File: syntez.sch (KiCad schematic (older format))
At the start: 14 parts, among them J12 USB_B_Mini, J15 IO, U1 SI5351A, Y2 Crystal

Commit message: add I2S_CLKIN_MCU
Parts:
- removed J12: USB_B_Mini, Connect:USB_Mini-B, symbol USB_B_Mini
- removed RN4: 47, Resistors_SMD:R_Array_Convex_4x0603, symbol R_Pack04
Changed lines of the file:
@@
 $Descr A4 11693 8268
 encoding utf-8
-Sheet 2 6
+Sheet 2 5
 Title ""
 Date ""
@@
 	3150 1500 3150 2250
 $Comp
-L +3V3 #PWR13
+L +3V3 #PWR011
 U 1 1 5DDEDF62
 P 3150 1500
-F 0 "#PWR13" H 3150 1350 50  0001 C CNN
+F 0 "#PWR011" H 3150 1350 50  0001 C CNN
 F 1 "+3V3" H 3150 1640 50  0000 C CNN
 F 2 "" H 3150 1500 50  0001 C CNN
@@
 	3000 2900 2550 2900
 $Comp
-L GND #PWR12
+L GND #PWR012
 U 1 1 5DDEE4A0
 P 2750 1800
-F 0 "#PWR12" H 2750 1550 50  0001 C CNN
+F 0 "#PWR012" H 2750 1550 50  0001 C CNN
 F 1 "GND" H 2750 1650 50  0001 C CNN
 F 2 "" H 2750 1800 50  0001 C CNN
@@
 $EndComp
 $Comp
-L GND #PWR14
+L GND #PWR013
 U 1 1 5DDEE4E1
 P 4750 2450
-F 0 "#PWR14" H 4750 2200 50  0001 C CNN
+F 0 "#PWR013" H 4750 2200 50  0001 C CNN
 F 1 "GND" H 4750 2300 50  0001 C CNN
 F 2 "" H 4750 2450 50  0001 C CNN
@@
 $EndComp
 $Comp
-L +3V3 #PWR15
+L +3V3 #PWR014
 U 1 1 5DDEE519
 P 4750 2550
-F 0 "#PWR15" H 4750 2400 50  0001 C CNN
+F 0 "#PWR014" H 4750 2400 50  0001 C CNN
 F 1 "+3V3" V 4750 2800 50  0000 C CNN
 F 2 "" H 4750 2550 50  0001 C CNN
@@
 Connection ~ 6100 1100
 $Comp
-L GND #PWR16
+L GND #PWR015
 U 1 1 5DDEEBF2
 P 6100 1400
-F 0 "#PWR16" H 6100 1150 50  0001 C CNN
+F 0 "#PWR015" H 6100 1150 50  0001 C CNN
 F 1 "GND" H 6100 1250 50  0001 C CNN
 F 2 "" H 6100 1400 50  0001 C CNN
@@
 $EndComp
 $Comp
-L GND #PWR17
+L GND #PWR016
 U 1 1 5DDEEC35
 P 6100 2150
-F 0 "#PWR17" H 6100 1900 50  0001 C CNN
+F 0 "#PWR016" H 6100 1900 50  0001 C CNN
 F 1 "GND" H 6100 2000 50  0001 C CNN
 F 2 "" H 6100 2150 50  0001 C CNN
@@
 	6100 2650 6100 2750
 $Comp
-L GND #PWR18
+L GND #PWR017
 U 1 1 5DDEECF7
 P 6100 2950
-F 0 "#PWR18" H 6100 2700 50  0001 C CNN
+F 0 "#PWR017" H 6100 2700 50  0001 C CNN
 F 1 "GND" H 6100 2800 50  0001 C CNN
 F 2 "" H 6100 2950 50  0001 C CNN
@@
 Text GLabel 8000 3600 0    60   Input ~ 0
 IO0
-Text GLabel 4400 6100 2    60   Input ~ 0
-I2C_SCL_MCU
-Text GLabel 4400 6300 2    60   BiDi ~ 0
-I2C_SDA_MCU
-Text GLabel 3200 5600 0    60   Output ~ 0
-I2C_SCL
-Text GLabel 3200 5800 0    60   BiDi ~ 0
-I2C_SDA
-$Comp
-L USB_B_Mini J12
-U 1 1 5DE4C0D6
-P 2200 6400
-F 0 "J12" H 2000 6850 50  0000 L CNN
-F 1 "USB_B_Mini" H 2000 6750 50  0000 L CNN
-F 2 "Connect:USB_Mini-B" H 2350 6350 50  0001 C CNN
-F 3 "" H 2350 6350 50  0001 C CNN
-	1    2200 6400
-	1    0    0    -1
-$EndComp
-Wire Wire Line
-	4200 6400 4200 6700
-Wire Wire Line
-	4200 6700 4400 6700
-Text GLabel 4400 6700 2    60   BiDi ~ 0
-USB_DM
-Text GLabel 4400 6500 2    60   BiDi ~ 0
-USB_DP
-$Comp
-L GND #PWR11
-U 1 1 5DE4C0F5
-P 2200 6900
-F 0 "#PWR11" H 2200 6650 50  0001 C CNN
-F 1 "GND" H 2200 6750 50  0000 C CNN
-F 2 "" H 2200 6900 50  0001 C CNN
-F 3 "" H 2200 6900 50  0001 C CNN
-	1    2200 6900
-	1    0    0    -1
-$EndComp
-$Comp
-L R_Pack04 RN4
-U 1 1 5DE4C1DE
-P 3850 6400
-F 0 "RN4" V 3550 6400 50  0000 C CNN
-F 1 "47" V 4050 6400 50  0000 C CNN
-F 2 "Resistors_SMD:R_Array_Convex_4x0603" V 4125 6400 50  0001 C CNN
-F 3 "" H 3850 6400 50  0001 C CNN
-	1    3850 6400
-	0    1    1    0
-$EndComp
-Wire Wire Line
-	4050 6500 4400 6500
-Wire Wire Line
-	4050 6300 4400 6300
-Wire Wire Line
-	3200 5800 3300 5800
-Wire Wire Line
-	3300 5800 3300 6300
-Wire Wire Line
-	3300 6300 3650 6300
-Wire Wire Line
-	2200 6800 2200 6900
-Wire Wire Line
-	2100 6800 2100 6850
-Wire Wire Line
-	2100 6850 2200 6850
-Connection ~ 2200 6850
-Wire Wire Line
-	3200 5600 3400 5600
-Wire Wire Line
-	3400 5600 3400 6200
-Wire Wire Line
-	3400 6200 3650 6200
-Wire Wire Line
-	4400 6100 4300 6100
-Wire Wire Line
-	4300 6100 4300 6200
-Wire Wire Line
-	4300 6200 4050 6200
-Wire Wire Line
-	4050 6400 4200 6400
-Wire Wire Line
-	3650 6400 3050 6400
-Wire Wire Line
-	3050 6400 3050 6500
-Wire Wire Line
-	3050 6500 2500 6500
-Wire Wire Line
-	2500 6400 2850 6400
-Wire Wire Line
-	2850 6400 2850 6600
-Wire Wire Line
-	2850 6600 3250 6600
-Wire Wire Line
-	3250 6600 3250 6500
-Wire Wire Line
-	3250 6500 3650 6500
 Wire Wire Line
 	4750 2250 5500 2250
@@
 	8250 5000 8000 5000
 $Comp
-L GND #PWR19
+L GND #PWR018
 U 1 1 5E9983F7
 P 9150 5100
-F 0 "#PWR19" H 9150 4850 50  0001 C CNN
+F 0 "#PWR018" H 9150 4850 50  0001 C CNN
 F 1 "GND" H 9150 4950 50  0001 C CNN
 F 2 "" H 9150 5100 50  0001 C CNN

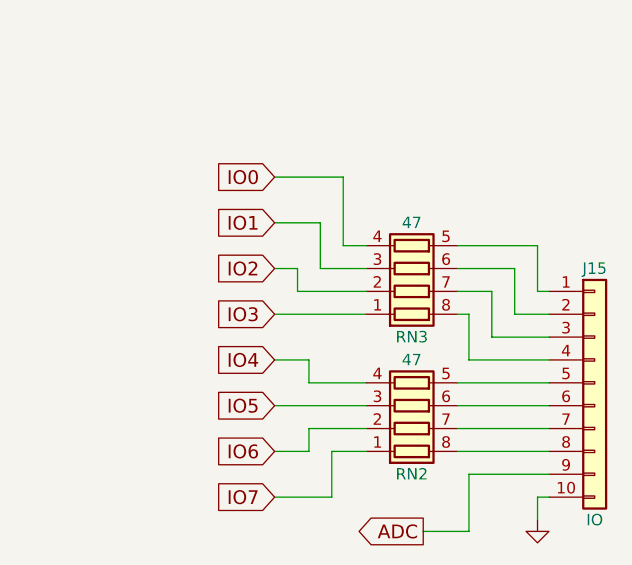
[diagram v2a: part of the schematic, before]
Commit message: PCB almost ready, needs some GND vias
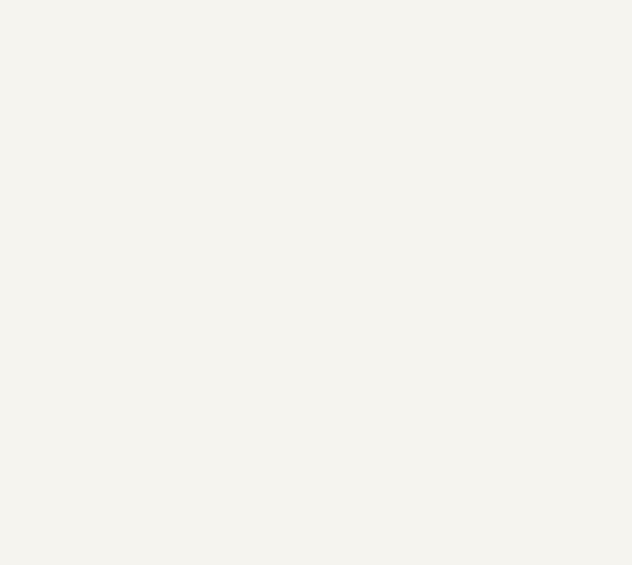
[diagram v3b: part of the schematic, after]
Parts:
- removed J15: IO, Pin_Headers:Pin_Header_Straight_1x10_Pitch2.54mm, symbol Conn_01x10
- removed RN2, RN3: 47, Resistors_SMD:R_Array_Convex_4x0603, symbol R_Pack04
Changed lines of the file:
@@
 CLK0
 Connection ~ 6100 2650
-$Comp
-L R_Pack04 RN3
-U 1 1 5DDF0BF3
-P 8600 4000
-F 0 "RN3" V 8300 4000 50  0000 C CNN
-F 1 "47" V 8800 4000 50  0000 C CNN
-F 2 "Resistors_SMD:R_Array_Convex_4x0603" V 8875 4000 50  0001 C CNN
-F 3 "" H 8600 4000 50  0001 C CNN
-	1    8600 4000
-	0    1    -1   0
-$EndComp
-Text GLabel 8000 4200 0    60   Input ~ 0
-IO3
-Text GLabel 8000 4000 0    60   Input ~ 0
-IO2
-Text GLabel 8000 3800 0    60   Input ~ 0
-IO1
-Text GLabel 8000 3600 0    60   Input ~ 0
-IO0
 Wire Wire Line
 	4750 2250 5500 2250
@@
 Wire Wire Line
 	3000 2200 3000 2350
-$Comp
-L Conn_01x10 J15
-U 1 1 5E9956FF
-P 9400 4500
-F 0 "J15" H 9400 5000 50  0000 C CNN
-F 1 "IO" H 9400 3900 50  0000 C CNN
-F 2 "Pin_Headers:Pin_Header_Straight_1x10_Pitch2.54mm" H 9400 4500 50  0001 C CNN
-F 3 "" H 9400 4500 50  0001 C CNN
-	1    9400 4500
-	1    0    0    -1
-$EndComp
-$Comp
-L R_Pack04 RN2
-U 1 1 5E996C05
-P 8600 4600
-F 0 "RN2" V 8300 4600 50  0000 C CNN
-F 1 "47" V 8800 4600 50  0000 C CNN
-F 2 "Resistors_SMD:R_Array_Convex_4x0603" V 8875 4600 50  0001 C CNN
-F 3 "" H 8600 4600 50  0001 C CNN
-	1    8600 4600
-	0    1    -1   0
-$EndComp
-Wire Wire Line
-	8800 4500 9200 4500
-Wire Wire Line
-	8800 4600 9200 4600
-Wire Wire Line
-	8800 4700 9200 4700
-Wire Wire Line
-	8800 4800 9200 4800
-Wire Wire Line
-	9200 4900 8850 4900
-Wire Wire Line
-	8850 4900 8850 5150
-Wire Wire Line
-	8850 5150 8650 5150
-Text GLabel 8650 5150 0    60   Output ~ 0
-ADC
-Text GLabel 8000 4400 0    60   Input ~ 0
-IO4
-Wire Wire Line
-	9200 4400 8850 4400
-Wire Wire Line
-	8850 4400 8850 4200
-Wire Wire Line
-	8850 4200 8800 4200
-Wire Wire Line
-	8800 4100 8950 4100
-Wire Wire Line
-	8950 4100 8950 4300
-Wire Wire Line
-	8950 4300 9200 4300
-Wire Wire Line
-	9200 4200 9050 4200
-Wire Wire Line
-	9050 4200 9050 4000
-Wire Wire Line
-	9050 4000 8800 4000
-Wire Wire Line
-	8800 3900 9150 3900
-Wire Wire Line
-	9150 3900 9150 4100
-Wire Wire Line
-	9150 4100 9200 4100
-Wire Wire Line
-	8300 3900 8400 3900
-Wire Wire Line
-	8300 3900 8300 3600
-Wire Wire Line
-	8300 3600 8000 3600
-Wire Wire Line
-	8000 3800 8200 3800
-Wire Wire Line
-	8200 3800 8200 4000
-Wire Wire Line
-	8200 4000 8400 4000
-Wire Wire Line
-	8000 4000 8100 4000
-Wire Wire Line
-	8100 4000 8100 4100
-Wire Wire Line
-	8100 4100 8400 4100
-Wire Wire Line
-	8000 4200 8400 4200
-Wire Wire Line
-	8000 4400 8150 4400
-Wire Wire Line
-	8150 4400 8150 4500
-Wire Wire Line
-	8150 4500 8400 4500
-Text GLabel 8000 4600 0    60   Input ~ 0
-IO5
-Text GLabel 8000 4800 0    60   Input ~ 0
-IO6
-Text GLabel 8000 5000 0    60   Input ~ 0
-IO7
-Wire Wire Line
-	8000 4600 8400 4600
-Wire Wire Line
-	8000 4800 8150 4800
-Wire Wire Line
-	8150 4800 8150 4700
-Wire Wire Line
-	8150 4700 8400 4700
-Wire Wire Line
-	8400 4800 8250 4800
-Wire Wire Line
-	8250 4800 8250 5000
-Wire Wire Line
-	8250 5000 8000 5000
-$Comp
-L GND #PWR018
-U 1 1 5E9983F7
-P 9150 5100
-F 0 "#PWR018" H 9150 4850 50  0001 C CNN
-F 1 "GND" H 9150 4950 50  0001 C CNN
-F 2 "" H 9150 5100 50  0001 C CNN
-F 3 "" H 9150 5100 50  0001 C CNN
-	1    9150 5100
-	1    0    0    -1
-$EndComp
-Wire Wire Line
-	9150 5100 9150 5000
-Wire Wire Line
-	9150 5000 9200 5000
 $EndSCHEMATC
